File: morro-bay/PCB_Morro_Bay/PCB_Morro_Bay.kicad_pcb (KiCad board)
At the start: 2 copper layers, 220 x 145.5 mm, 346 parts, among them J1 POWER, J10 5V_12_8, J11 5V_12_9, J12 5V_12_10, J13 5V_12_11, J14 5V_12_12, J15 5V_12_13, J16 5V_12_14, J17 10V_12_1, J18 10V_12_2, J19 10V_12_3, J2 CAN, J20 10V_12_4, J21 10V_12_5, J22 10V_12_6, J23 POWER_OUT, J24 5V_16_1, J25 5V_16_2, J26 5V_16_3, J27 5V_16_4, J28 10V_16_1, J29 10V_16_2, J3 5V_12_1, J30 10V_16_3, J31 10V_16_4, J32 5V_16_5, J33 5V_16_6, J34 5V_16_7, J35 5V_16_8, J36 SWD, J37 GPIO, J38 USB_B, J39 ESERCOM, J4 5V_12_2, J5 5V_12_3, J6 5V_12_4, J7 5V_12_5, J8 5V_12_6, J9 5V_12_7, SW1 INPUT_RANGE_SEL_1, SW2 INPUT_RANGE_SEL_2, SW3 RESET, SW4 INPUT_RANGE_SEL_3, U1 MCP2515-xSO, U10 LM2902, U11 LM2902, U12 LM2902, U13 V7805-2000R, U2 SN65HVD232, U26 ADS114S08BIPBSR, U3 AZ1117-3.3, U4 ATSAMD21J18A-AU, U5 LM2902, U6 LM2902, U7 LM2902, U8 LM2902, U9 LM2902, Y1 8MHz, Y2 30MHz, Y3 32.768kHz

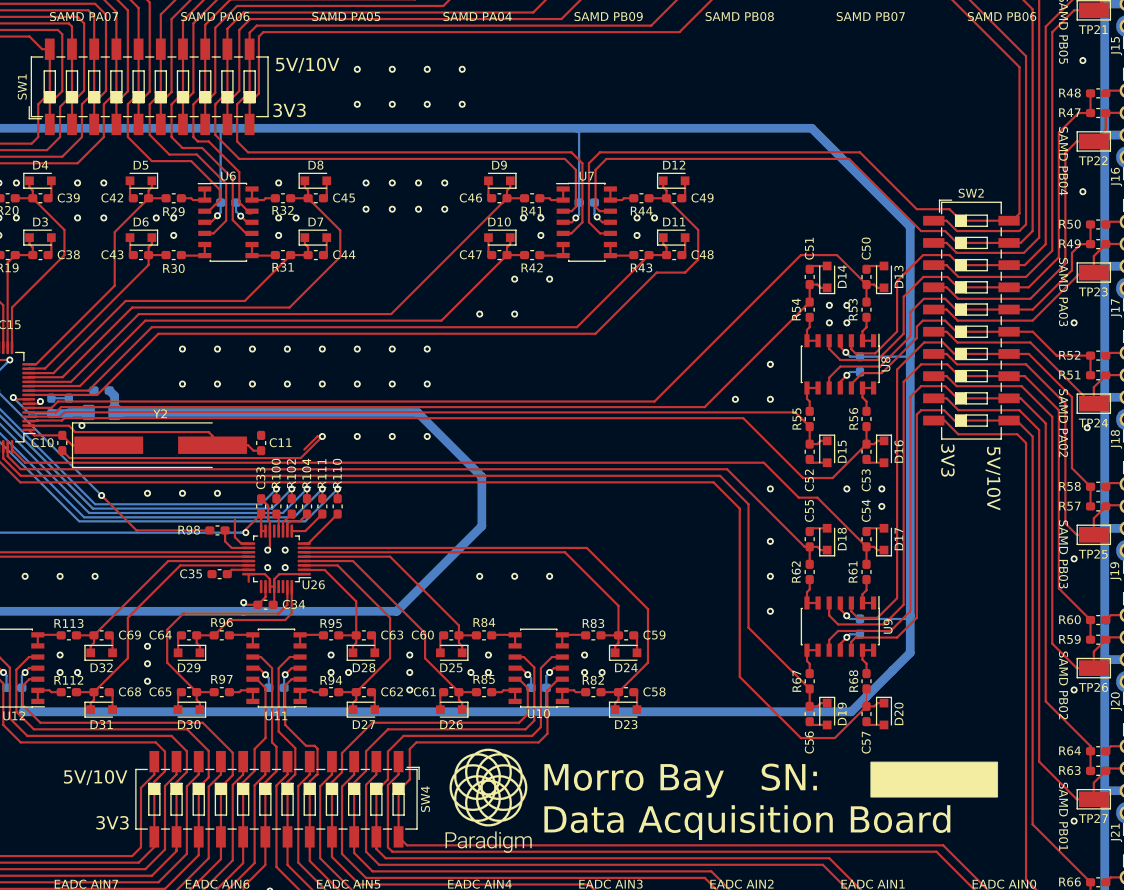
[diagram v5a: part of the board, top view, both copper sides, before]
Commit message: Add 3D models for connectors
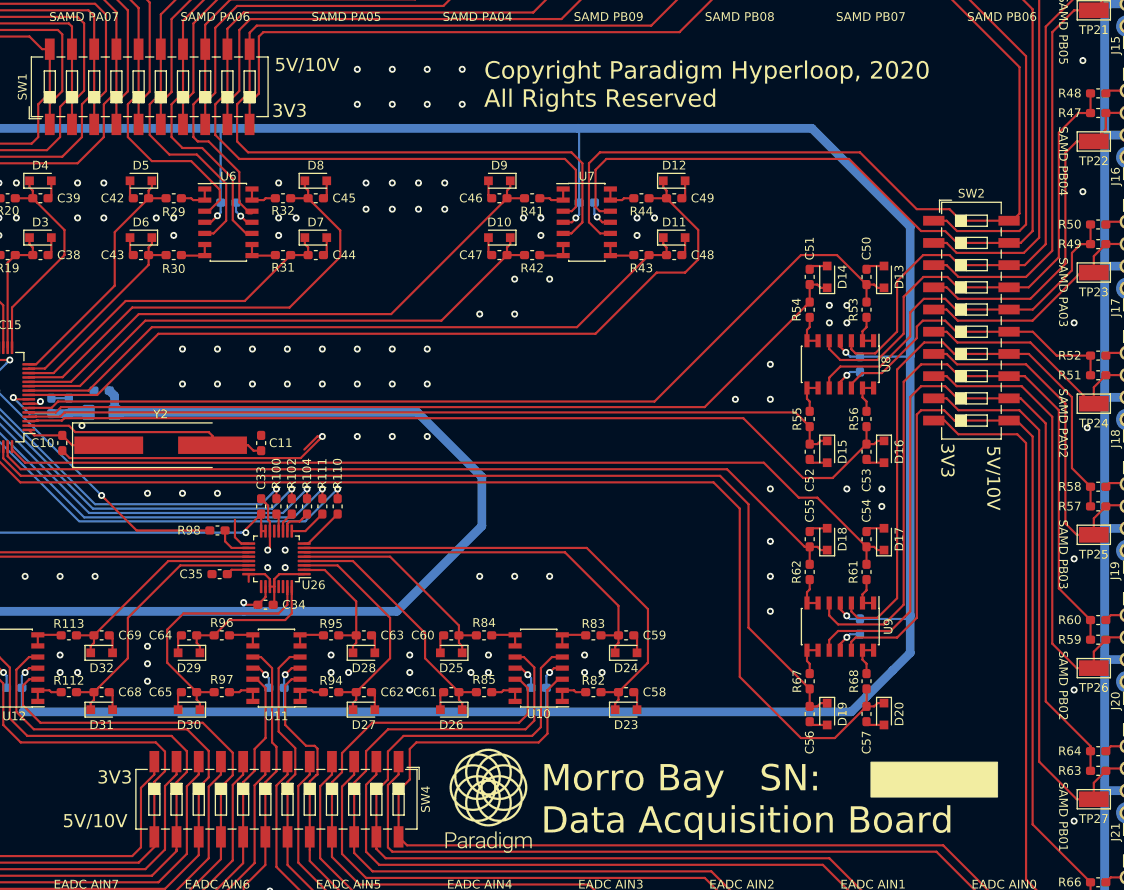
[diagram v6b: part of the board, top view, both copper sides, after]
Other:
- board text added: "Copyright Paradigm Hyperloop, 2020 All Rights Reserved"
